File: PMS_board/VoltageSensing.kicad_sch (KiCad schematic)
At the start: 29 parts, among them U3 Opamp_Quad, U4 Opamp_Quad, U5 Opamp_Quad

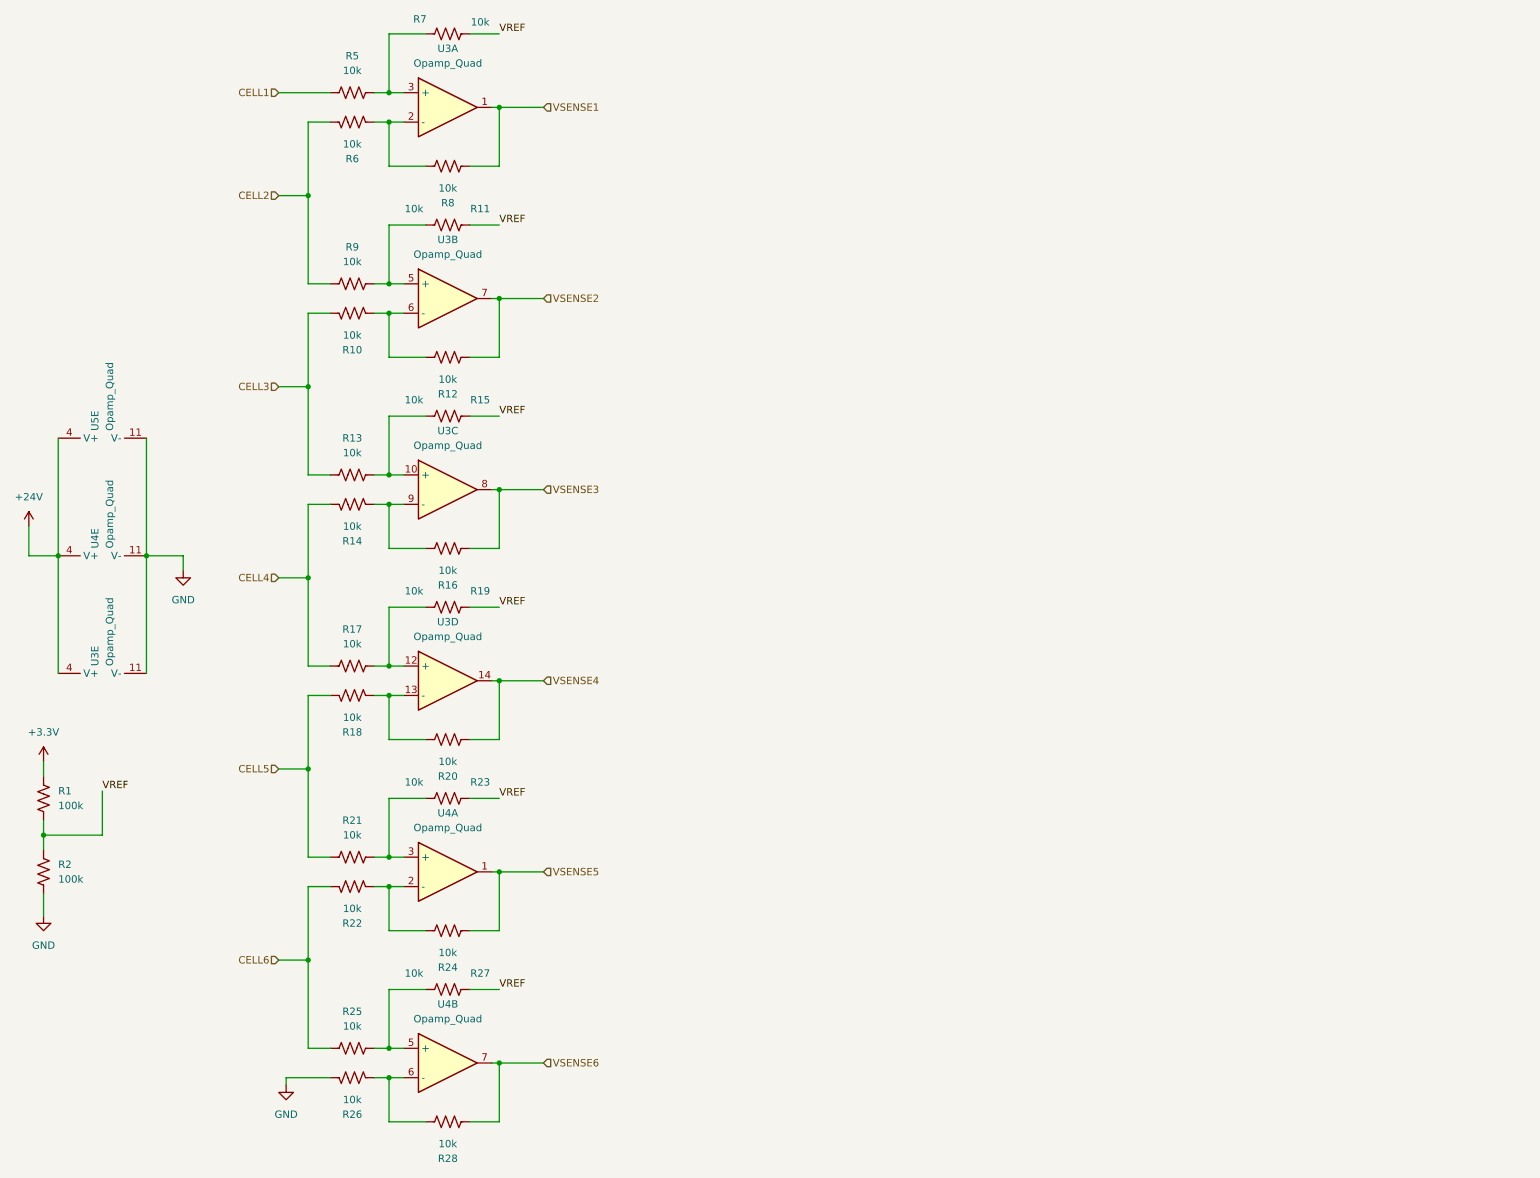
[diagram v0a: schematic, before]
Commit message: Add Cell connectors
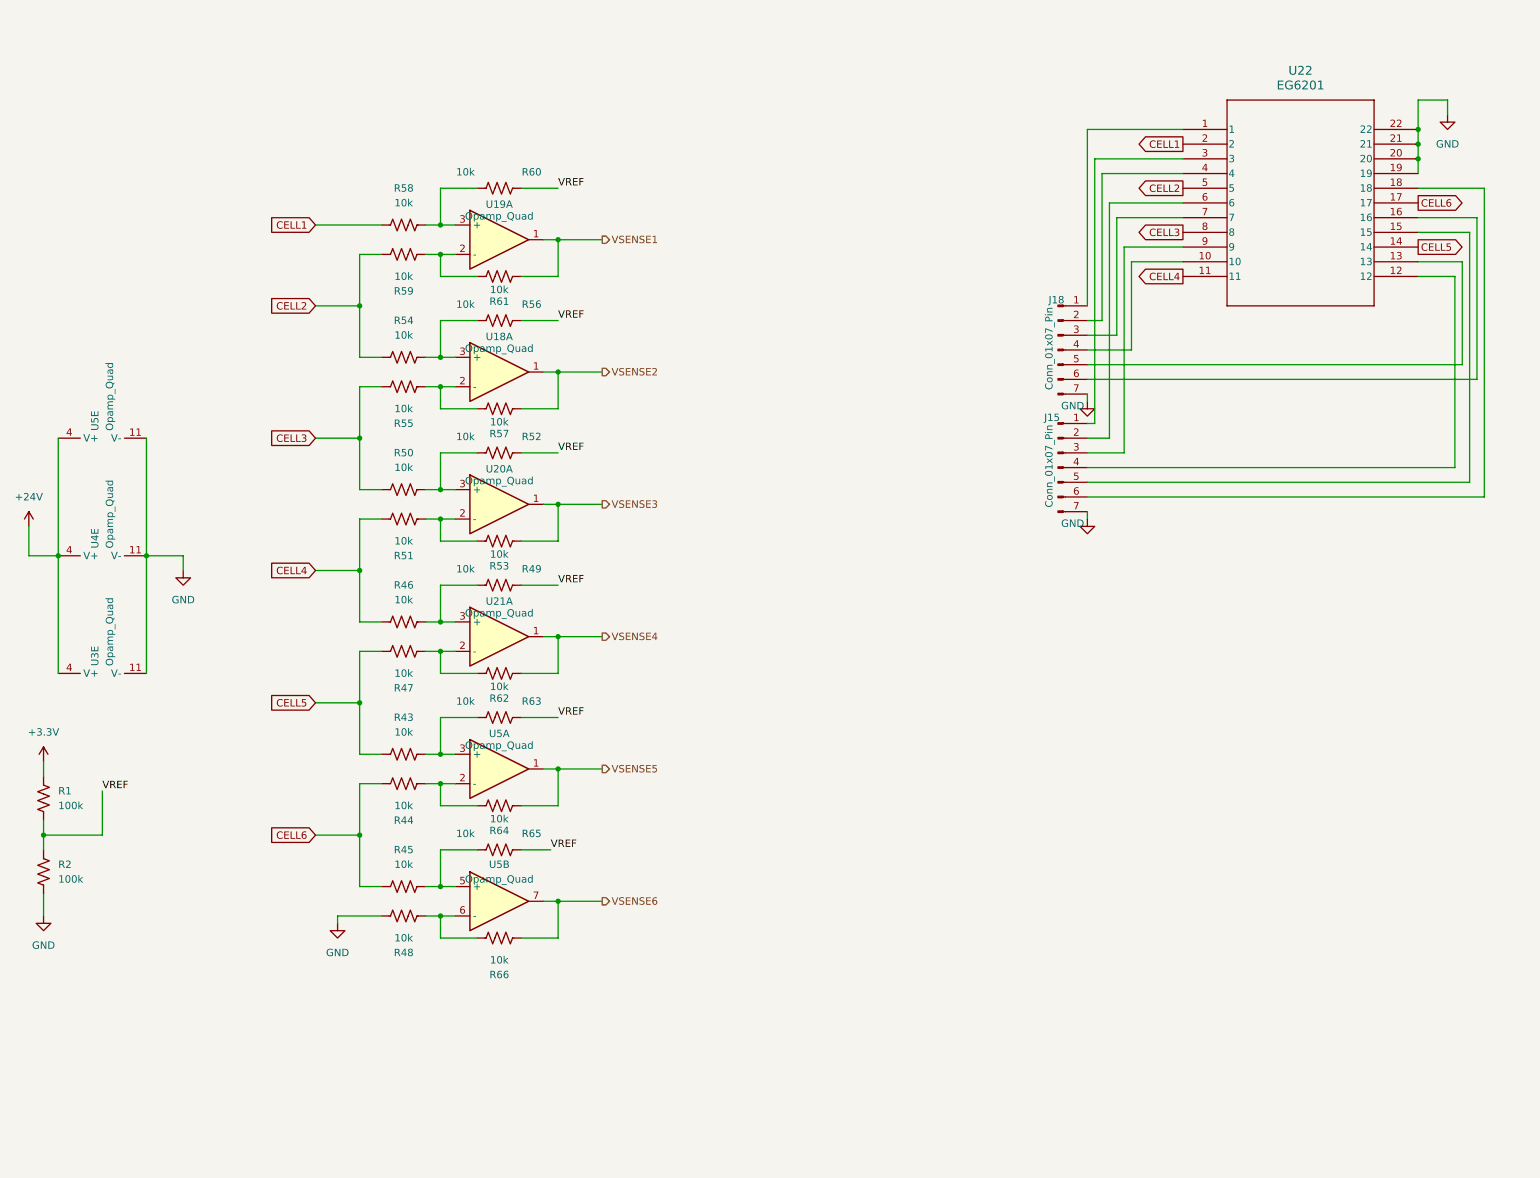
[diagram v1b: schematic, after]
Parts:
- removed R10, R11, R12, R13, R14, R15, R16, R17, R18, R19, R20, R21, R22, R23, R24, R25, R26, R27, R28, R5, R6, R7, R8, R9: 10k, symbol Device:R_US
- removed unit 3 of U3
- removed unit 2 of U3
- removed unit 4 of U3
- removed unit 1 of U3
- removed unit 2 of U4
- removed unit 1 of U4
- added J15, J18: Conn_01x07_Pin, Converter_DCDC:Converter_DCDC_Cyntec_MUN12AD01-SH, symbol Connector:Conn_01x07_Pin
- added R43, R44, R45, R46, R47, R48, R49, R50, R51, R52, R53, R54, R55, R56, R57, R58, R59, R60, R61, R62, R63, R64, R65, R66: 10k, symbol Device:R_US
- added U18, U19, U20, U21: Opamp_Quad, symbol Amplifier_Operational:Opamp_Quad
- added U22: EG6201, DIP_G6201_EWI, symbol EG6201:EG6201
- added unit 2 of U5
- added unit 1 of U5
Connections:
- net CELL1: now also R58.1, U22.2
- net CELL2: now also R54.1, R59.2, U22.5
- net CELL3: now also R50.1, R55.2, U22.8
- net CELL4: now also R46.1, R51.2, U22.11
- net CELL5: now also R43.1, R47.2, U22.14
- net CELL6: now also R44.2, R45.1, U22.17
- net GND: now also J15.7 (Pin_7), J18.7 (Pin_7), R48.2, U22.19, U22.20, U22.21, U22.22
- net VREF: now also R49.1, R52.1, R56.1, R60.1, R63.1, R65.1
- net VSENSE1: now also R61.2, U19.1
- net VSENSE2: now also R57.2, U18.1
- net VSENSE3: now also R53.2, U20.1
- net VSENSE4: now also R62.2, U21.1
- net VSENSE5: now also R64.2, U5.1
- net VSENSE6: now also R66.2, U5.7
- new net: R50.2, R52.2, U20.3 (+)
- new net: R43.2, R63.2, U5.3 (+)
- new net: R44.1, R64.1, U5.2 (-)
- new net: J18.1 (Pin_1), U22.1
- new net: J18.4 (Pin_4), U22.10
- new net: J15.4 (Pin_4), U22.12
- new net: J18.5 (Pin_5), U22.13
- new net: J15.5 (Pin_5), U22.15
- new net: J18.6 (Pin_6), U22.16
- new net: J15.6 (Pin_6), U22.18
- new net: J15.1 (Pin_1), U22.3
- new net: J18.2 (Pin_2), U22.4
- new net: J15.2 (Pin_2), U22.6
- new net: J18.3 (Pin_3), U22.7
- new net: J15.3 (Pin_3), U22.9
- new net: R51.1, R53.1, U20.2 (-)
- new net: R45.2, R65.2, U5.5 (+)
- new net: R48.1, R66.1, U5.6 (-)
- new net: R55.1, R57.1, U18.2 (-)
- new net: R54.2, R56.2, U18.3 (+)
- new net: R47.1, R62.1, U21.2 (-)
- new net: R46.2, R49.2, U21.3 (+)
- new net: R59.1, R61.1, U19.2 (-)
- new net: R58.2, R60.2, U19.3 (+)

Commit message: Swapped 3.3V in jeteson output rail with 3.3V (Jetson)
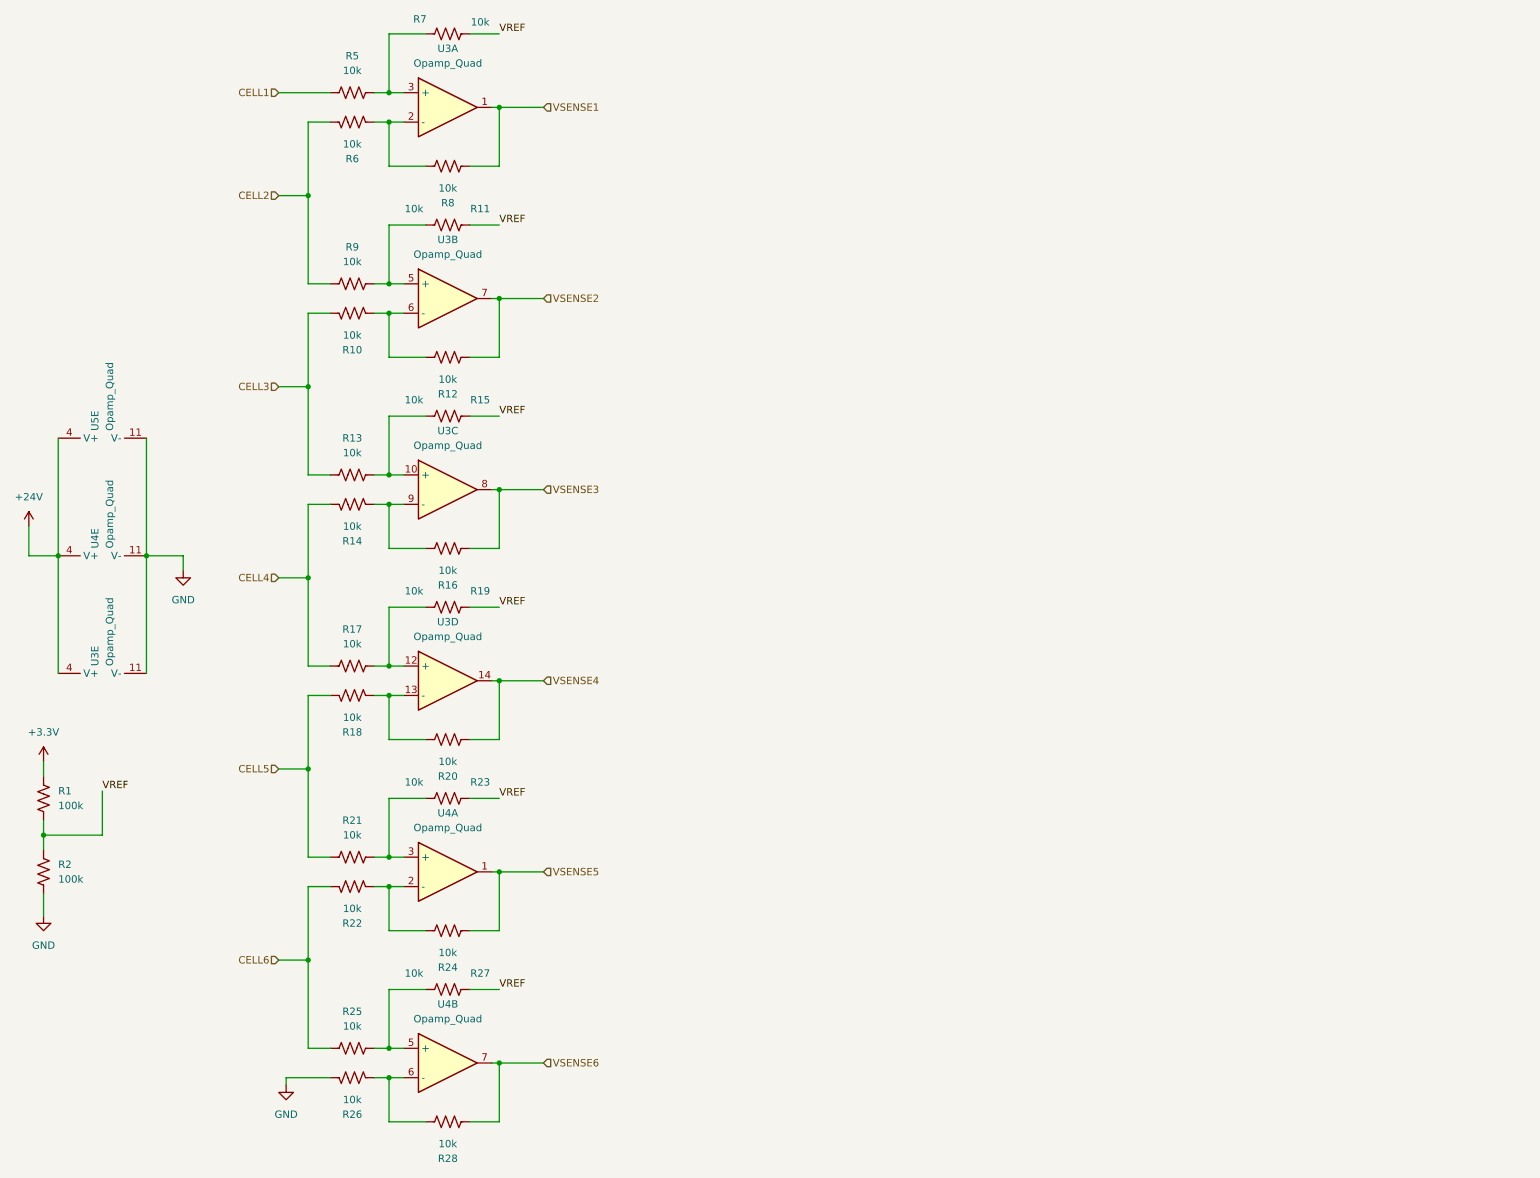
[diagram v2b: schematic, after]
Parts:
- removed J15, J18: Conn_01x07_Pin, Converter_DCDC:Converter_DCDC_Cyntec_MUN12AD01-SH, symbol Connector:Conn_01x07_Pin
- removed R43, R44, R45, R46, R47, R48, R49, R50, R51, R52, R53, R54, R55, R56, R57, R58, R59, R60, R61, R62, R63, R64, R65, R66: 10k, symbol Device:R_US
- removed U18, U19, U20, U21: Opamp_Quad, symbol Amplifier_Operational:Opamp_Quad
- removed U22: EG6201, DIP_G6201_EWI, symbol EG6201:EG6201
- removed unit 2 of U5
- removed unit 1 of U5
- added R10, R11, R12, R13, R14, R15, R16, R17, R18, R19, R20, R21, R22, R23, R24, R25, R26, R27, R28, R5, R6, R7, R8, R9: 10k, symbol Device:R_US
- added unit 3 of U3
- added unit 2 of U3
- added unit 4 of U3
- added unit 1 of U3
- added unit 2 of U4
- added unit 1 of U4
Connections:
- net CELL1: now also R5.1
- net CELL2: now also R6.1, R9.1
- net CELL3: now also R10.1, R13.1
- net CELL4: now also R14.1, R17.1
- net CELL5: now also R18.1, R21.1
- net CELL6: now also R22.1, R25.1
- net GND: now also R26.1
- net VREF: now also R11.1, R15.1, R19.1, R23.1, R27.1, R7.1
- net VSENSE1: now also R8.2, U3.1
- net VSENSE2: now also R12.2, U3.7
- net VSENSE3: now also R16.2, U3.8
- net VSENSE4: now also R20.2, U3.14
- net VSENSE5: now also R24.2, U4.1
- net VSENSE6: now also R28.2, U4.7
- new net: R25.2, R27.2, U4.5 (+)
- new net: R26.2, R28.1, U4.6 (-)
- new net: R14.2, R16.1, U3.9 (-)
- new net: R18.2, R20.1, U3.13 (-)
- new net: R17.2, R19.2, U3.12 (+)
- new net: R21.2, R23.2, U4.3 (+)
- new net: R13.2, R15.2, U3.10 (+)
- new net: R22.2, R24.1, U4.2 (-)
- new net: R11.2, R9.2, U3.5 (+)
- new net: R10.2, R12.1, U3.6 (-)
- new net: R5.2, R7.2, U3.3 (+)
- new net: R6.2, R8.1, U3.2 (-)
